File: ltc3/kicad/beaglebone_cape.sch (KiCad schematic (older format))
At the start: 8 parts, among them U501 24C256

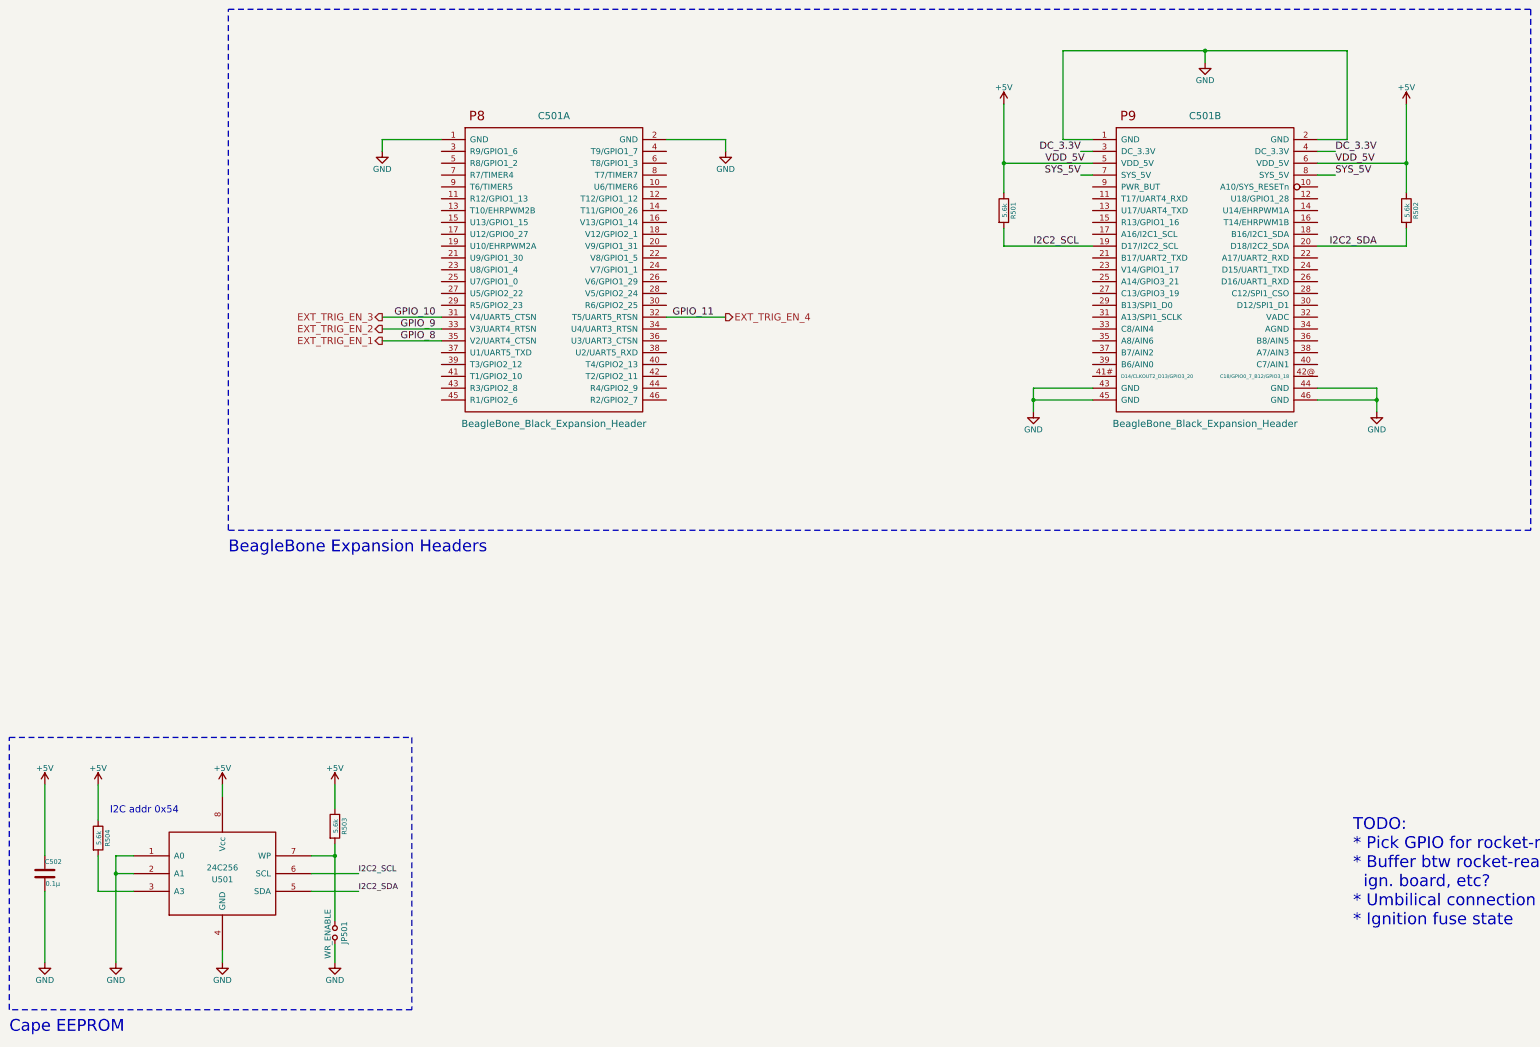
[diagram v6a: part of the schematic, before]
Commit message: LTC3: Cleaned up I2C devices.
Gave each power sub-circuit its own LTC299x sensor.  Charger and
battery pack circuits each get an LTC2990 (quad); DC-DC converter
circuit gets an LTC2991 (octal).

Separate sensor ICs for each sub-circuit allows the chip to be as
close to its sense resistors as possible (and makes for a cleaner
schematic).
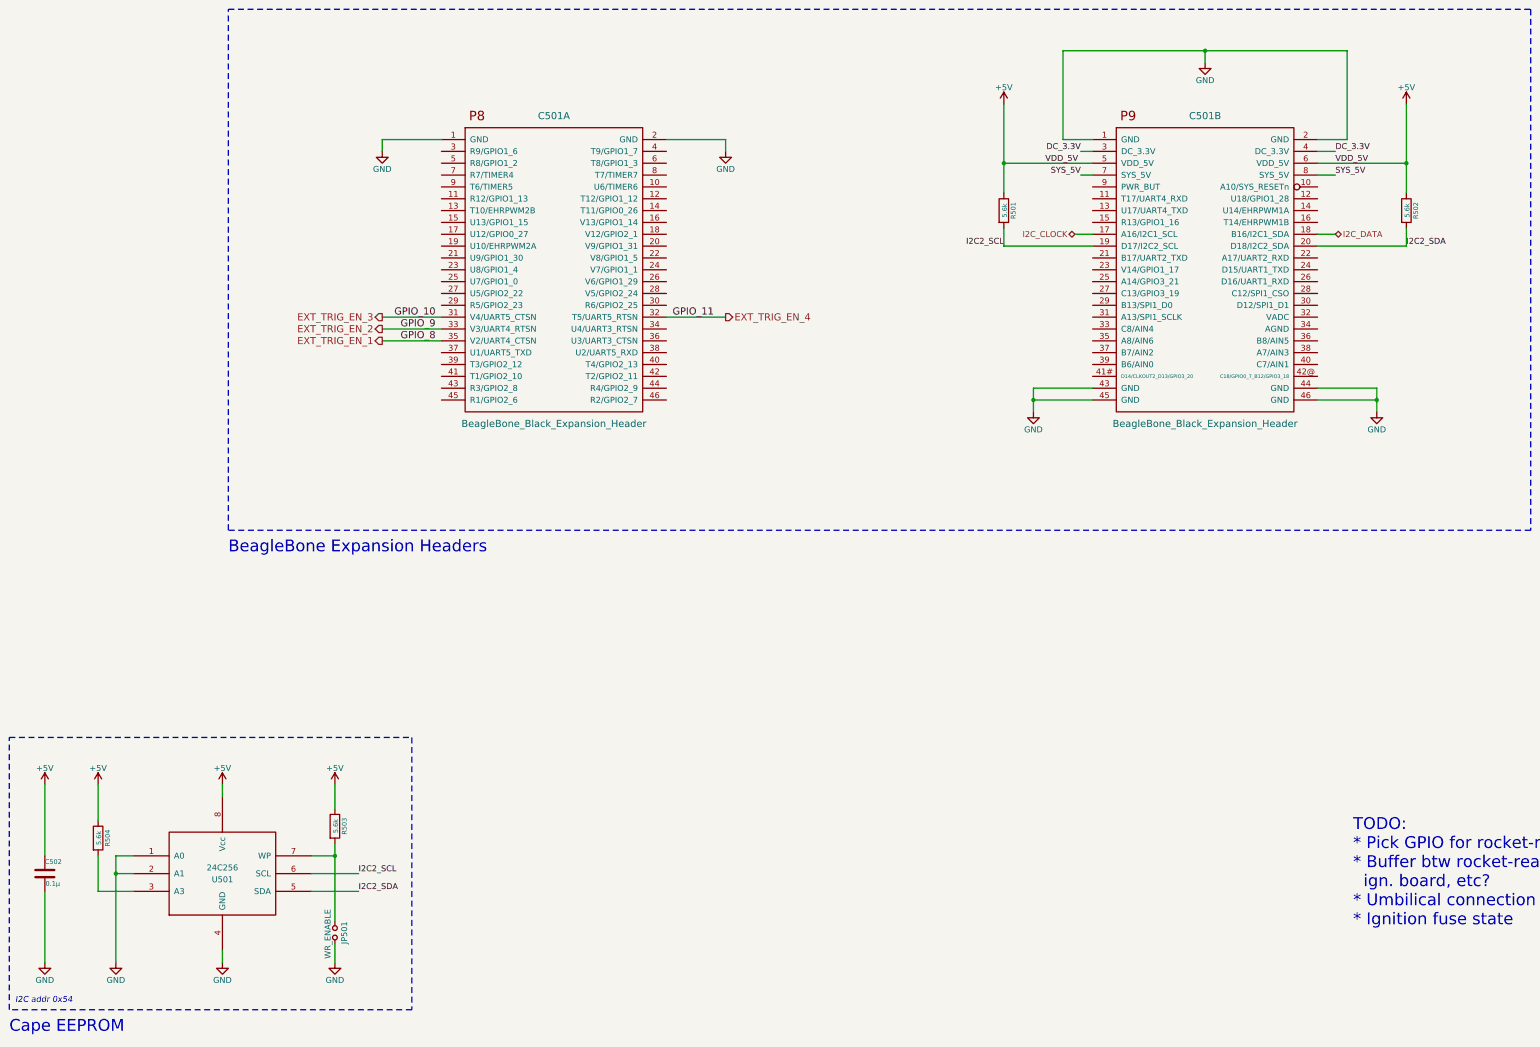
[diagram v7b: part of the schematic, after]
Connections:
- net I2C_CLOCK: now reaches C501.17 (A16/I2C1_SCL)
- net I2C_DATA: now reaches C501.18 (B16/I2C1_SDA)
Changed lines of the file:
@@
 EESchema Schematic File Version 2
+LIBS:BeagleBone_Black
+LIBS:LT8490
+LIBS:LTC299x
+LIBS:PMV45EN
+LIBS:PTN78020n
+LIBS:EEPROMs
+LIBS:TLP
+LIBS:bq77PL900
+LIBS:current_shunt
+LIBS:741g08
+LIBS:4n35
+LIBS:SNx52x0
+LIBS:switches
+LIBS:CD74HC14
+LIBS:power_nodes
+LIBS:relay_1c
 LIBS:power
 LIBS:device
@@
 LIBS:contrib
 LIBS:valves
-LIBS:BeagleBone_Black
-LIBS:LT8490
-LIBS:LTC299x
-LIBS:PMV45EN
-LIBS:PTN78020n
-LIBS:EEPROMs
-LIBS:TLP
-LIBS:bq77PL900
-LIBS:current_shunt
-LIBS:741g08
-LIBS:4n35
-LIBS:SNx52x0
-LIBS:switches
-LIBS:CD74HC14
-LIBS:power_nodes
-LIBS:relay_1c
 LIBS:Launch_Tower_Computer_III-cache
 EELAYER 25 0
@@
 $Descr B 17000 11000
 encoding utf-8
-Sheet 3 7
+Sheet 5 7
 Title "LTC3 BeagleBone Black Cape Interface"
 Date "2015-11-25"
@@
 	1    0    0    -1
 $EndComp
-Text Label 9600 3400 0    60   ~ 0
+Text Label 9350 3400 2    50   ~ 0
 I2C2_SCL
-Text Label 12500 3400 2    60   ~ 0
+Text Label 12750 3400 0    50   ~ 0
 I2C2_SDA
-Text Label 10000 2600 2    60   ~ 0
+Text Label 10000 2600 2    50   ~ 0
 DC_3.3V
-Text Label 9700 2700 0    60   ~ 0
+Text Label 9700 2700 0    50   ~ 0
 VDD_5V
-Text Label 10000 2800 2    60   ~ 0
+Text Label 10000 2800 2    50   ~ 0
 SYS_5V
 Text Notes 950  10050 0    100  ~ 0
@@
 	3500 8700 3900 8700
 Wire Wire Line
-	3700 8450 3700 8550
-Wire Wire Line
-	3700 8550 3700 9100
+	3700 8450 3700 9100
 Wire Wire Line
 	3500 8550 3700 8550
@@
 	2000 8700 1850 8700
 Wire Wire Line
-	1850 8550 1850 8700
-Wire Wire Line
-	1850 8700 1850 9450
+	1850 8550 1850 9450
 Wire Wire Line
 	2000 8550 1850 8550
@@
 $EndComp
 Wire Wire Line
-	9600 4600 9600 4700
-Wire Wire Line
-	9600 4700 9600 4800
+	9600 4600 9600 4800
 Wire Wire Line
 	9600 4700 10100 4700
@@
 $EndComp
 Wire Wire Line
-	12500 4600 12500 4700
-Wire Wire Line
-	12500 4700 12500 4800
+	12500 4600 12500 4800
 Wire Wire Line
 	12500 4700 12000 4700
@@
 Wire Wire Line
 	12750 2700 12000 2700
-Text Label 12150 2700 0    60   ~ 0
+Text Label 12150 2700 0    50   ~ 0
 VDD_5V
-Text Label 12150 2600 0    60   ~ 0
+Text Label 12150 2600 0    50   ~ 0
 DC_3.3V
 Wire Wire Line
@@
 	9850 2500 9850 1750
 Wire Wire Line
-	9850 1750 11050 1750
-Wire Wire Line
-	11050 1750 12250 1750
+	9850 1750 12250 1750
 Wire Wire Line
 	11050 1750 11050 1850
@@
 Wire Wire Line
 	10000 2800 10100 2800
-Text Label 12150 2800 0    60   ~ 0
+Text Label 12150 2800 0    50   ~ 0
 SYS_5V
 Wire Wire Line
@@
 $EndComp
 Wire Wire Line
-	12750 2200 12750 2700
-Wire Wire Line
-	12750 2700 12750 2950
+	12750 2200 12750 2950
 $Comp
 L +5V #PWR502
@@
 $EndComp
 Wire Wire Line
-	9350 2200 9350 2700
-Wire Wire Line
-	9350 2700 9350 2950
+	9350 2200 9350 2950
 $Comp
 L +5V #PWR508
@@
 	1    0    0    -1
 $EndComp
-Text Notes 1800 8200 0    60   ~ 0
+Text Notes 1000 9800 0    50   Italic 0
 I2C addr 0x54
 $Comp
@@
 Text Notes 2800 6000 0    100  ~ 0
 BeagleBone Expansion Headers
+Text HLabel 9950 3300 0    50   BiDi ~ 0
+I2C_CLOCK
+Wire Wire Line
+	9950 3300 10100 3300
+Wire Wire Line
+	12000 3300 12150 3300
+Text HLabel 12150 3300 2    50   BiDi ~ 0
+I2C_DATA
 $EndSCHEMATC
